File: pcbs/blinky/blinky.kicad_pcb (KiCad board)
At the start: 4 copper layers, 91 x 93 mm, 182 parts, among them J1 JACK IN, J3 CA1-9, J4 CB1-9, Q1 PMBT2222A,215, SW1 TACTILE, SW2 JS202011JCQN, U1 ATSAMD21E17, U2 MIC5225-3.3YM5, U3 TSOP36438TT, U4 IS31FL3731-SALS2

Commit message: lovely logo
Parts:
- added LOGO1: Future, Joels KiCad Footprint Library:logo-future, F.Cu at (71.8, 94.8)
- added LOGO2: Future, Joels KiCad Footprint Library:logo-turtles, F.Cu at (93.0, 94.8)
- C1: value 100uF 6.3V -> 100u
- C10, C11: value 10uF -> 10u
- C2, C7: value 1uF -> 1u
- C3, C4, C8, C9: value 0.1uF -> 0.1u
- C5: value 1.0uF -> 1.0u
- C6: value 2.2uF -> 2.2u
- R1: value 10kΩ -> 10K
- R2: value 330Ω -> 330
- R3: value 47Ω -> 47
- R4: value 470Ω -> 470

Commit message: more details
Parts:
- added FID1: Fiducial, Fiducial:Fiducial_1mm_Mask3mm, F.Cu at (131.2, 109.3)
- added FID2: Fiducial, Fiducial:Fiducial_1mm_Mask3mm, F.Cu at (44.2, 92.3)
- added FID3: Fiducial, Fiducial:Fiducial_1mm_Mask3mm, F.Cu at (44.2, 145.3)
- added H5: MountingHole, Joels KiCad Footprint Library:JCLPCB_Tooling_Hole, F.Cu at (131.2, 74.3)
- added H6: MountingHole, Joels KiCad Footprint Library:JCLPCB_Tooling_Hole, F.Cu at (131.2, 157.3)
- added H7: MountingHole, Joels KiCad Footprint Library:JCLPCB_Tooling_Hole, F.Cu at (44.2, 74.3)
- added H8: MountingHole, Joels KiCad Footprint Library:JCLPCB_Tooling_Hole, F.Cu at (44.2, 157.3)
- added H9: Lanyard Hole, MountingHole:MountingHole_2.5mm_Pad_Via, F.Cu at (82.0, 73.3)
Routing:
- net /SWCLK: track 39.1 -> 61.4 mm, vias 1 -> 2
- net /SWDIO: track 41.5 -> 58.7 mm, vias 1 -> 2
- net /A7: track 46.1 -> 44.9 mm, vias 0 -> 2
- net /~RESET: track 15.2 -> 15.0 mm, vias 1 -> 2
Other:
- board text added: "JLCJLCJLCJLC"
- board text added: "WAKING DREAMS"

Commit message: ok, well that has been sent to china
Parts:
- H9: value Lanyard Hole -> Lanyard
- moved H9 1.47 mm to (81.8, 74.8)
- moved LOGO2 0.30 mm to (92.7, 94.8)
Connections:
- H9 pad 1: (no net) -> GND
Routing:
- net GND: track 111.7 -> 420.8 mm, vias 13 -> 14
- net (no net): track 270.2 -> 0.00 mm
- net +3V3: track 107.5 -> 50.3 mm
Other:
- board text added: "SECOND PROTOTYPE 12/31/21"

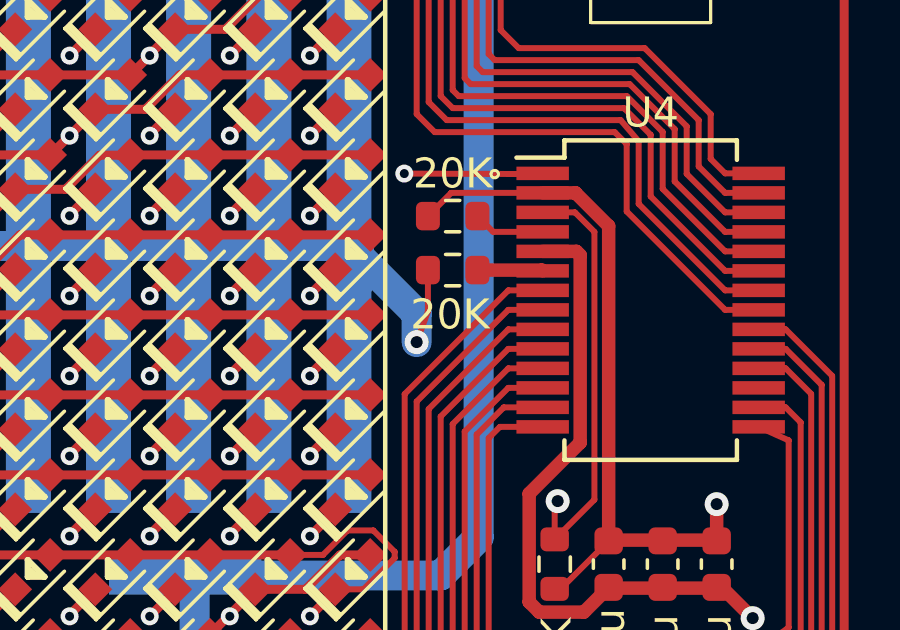
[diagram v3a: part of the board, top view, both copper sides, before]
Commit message: Use 100K resistor for Rext to save power
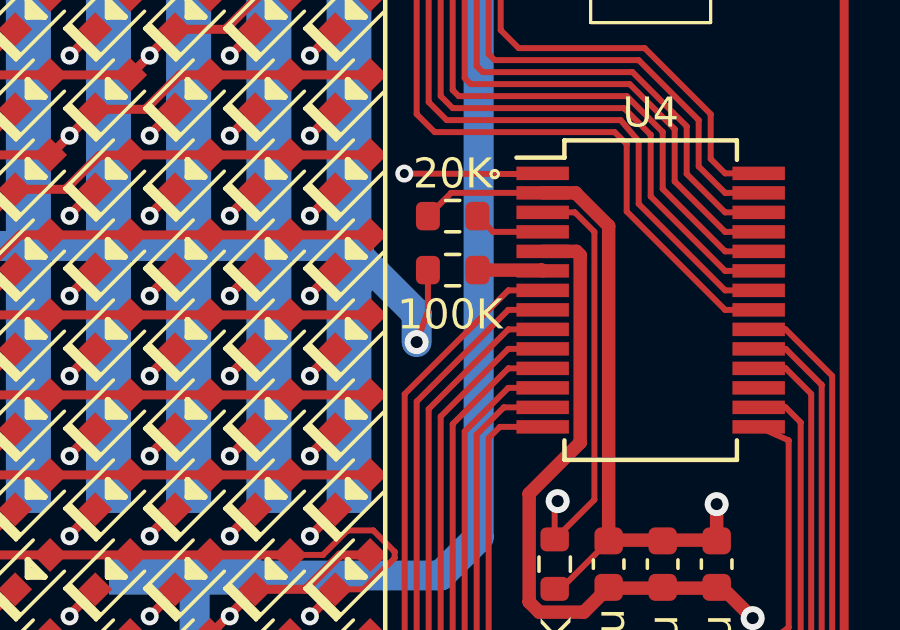
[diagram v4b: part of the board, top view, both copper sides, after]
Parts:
- R5: value 20K -> 100K

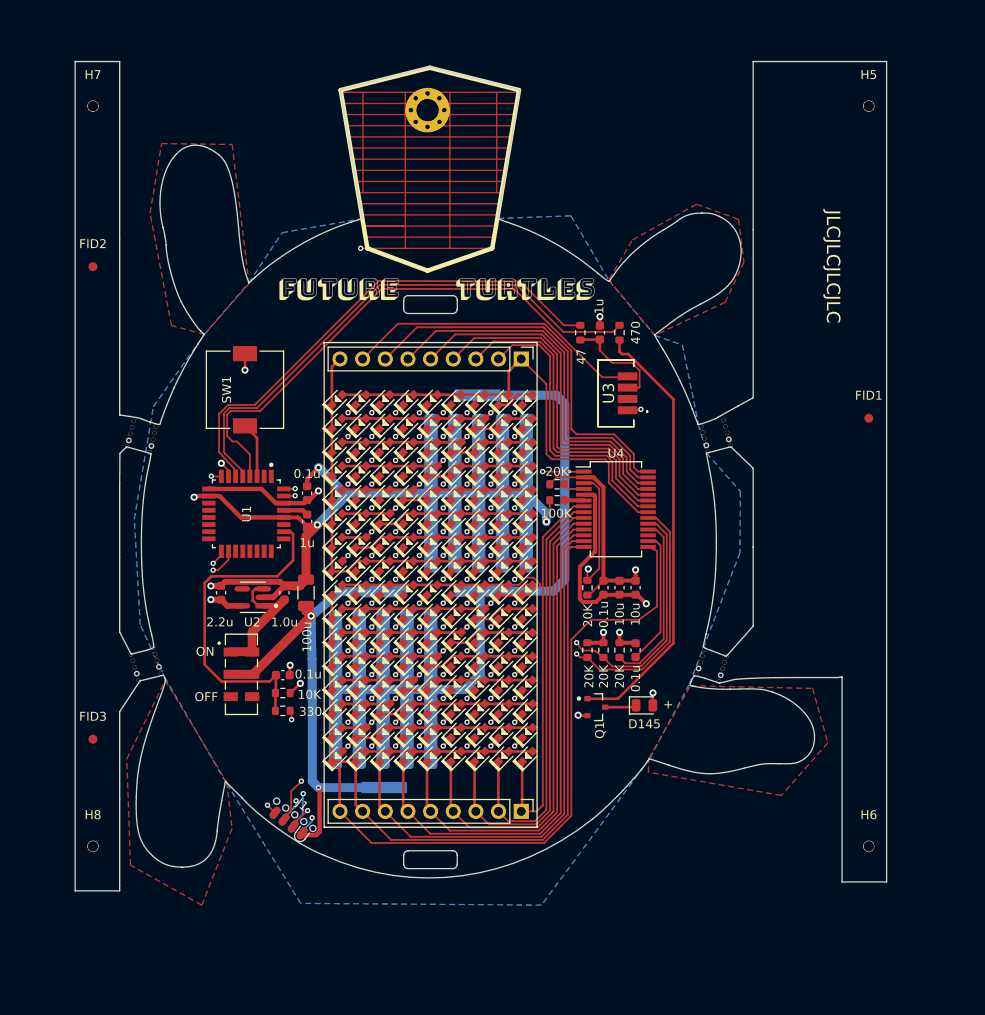
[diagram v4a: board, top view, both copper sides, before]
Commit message: Updated schematics and PCB to fix all known bugs
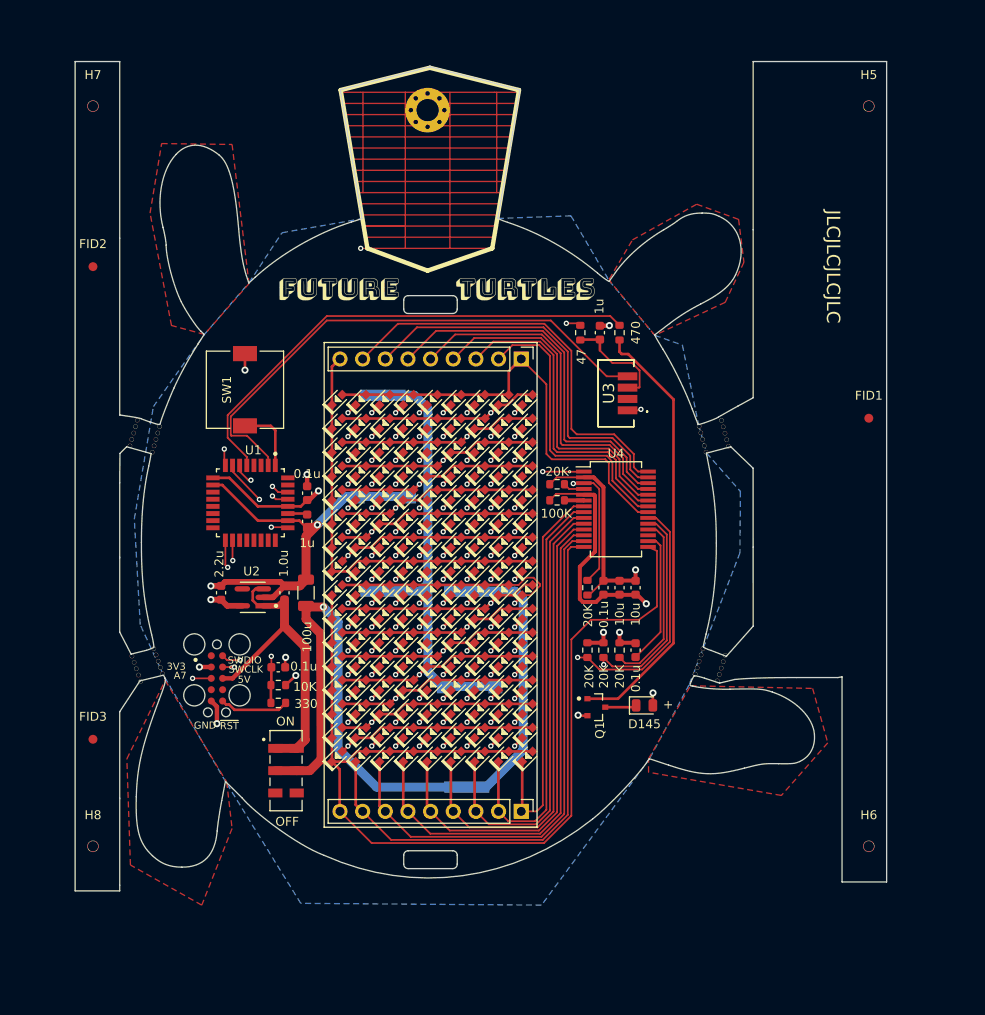
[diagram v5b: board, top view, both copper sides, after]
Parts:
- removed J1: JACK IN, Joels KiCad Footprint Library:SOIC_clipProgSmall
- added BT3: CR2032 (+) CLIP, Joels KiCad Footprint Library:BatteryHolder_Keystone_3034_Pos_Clip, B.Cu at (76.7, 117.7)
- added BT4: CR2032 (-) PAD, Joels KiCad Footprint Library:Keystone_2992_Negative_Contact_Pad, B.Cu at (80.8, 117.1)
- added J2: TC2050-IDC, Joels KiCad Footprint Library:TAG-CONNECT_TC2050-IDC, F.Cu at (58.1, 138.5)
- BT1: value CR2032 -> CR2032 (+) CLIP; footprint Joels KiCad Footprint Library:BatteryHolder_Keystone_3034_Minimum_Pad -> Joels KiCad Footprint Library:BatteryHolder_Keystone_3034_Pos_Clip
- BT2: value CR2032 -> CR2032 (-) PAD; footprint Joels KiCad Footprint Library:BatteryHolder_Keystone_3034_Minimum_Pad -> Joels KiCad Footprint Library:Keystone_2992_Negative_Contact_Pad
- U1: value ATSAMD21E17 -> ATSAMD21E17L-AF
- moved BT2 23.2 mm to (82.4, 140.4), turned to 0 degrees
- moved SW2 11.9 mm to (65.9, 148.8)
- moved BT1 9.25 mm to (86.1, 139.7), turned to 270 degrees
- moved U1 1.32 mm to (61.9, 118.8)
- moved C4 1.02 mm to (65.0, 137.2)
- moved R1 1.02 mm to (65.0, 139.2)
- moved R2 1.02 mm to (65.0, 141.2)
- moved H1 0.41 mm to (51.9, 109.5), turned to 74 degrees
- moved H3 0.24 mm to (114.5, 108.8)
- moved H4 0.18 mm to (115.3, 135.2)
- moved H2 0.12 mm to (50.8, 134.4), turned to 109 degrees
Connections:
- BT2 pad 1: Net-(BT1-Pad2) -> Net-(BT2-Pad1)
- U1 pad 1: Net-(U1-Pad1) -> /A0
- U1 pad 2: Net-(U1-Pad2) -> /A1
- U1 pad 25: Net-(U1-Pad25) -> /2RST
- U1 pad 26: /2RST -> GND
- U1 pad 27: Net-(U1-Pad27) -> /VDDCORE
- U1 pad 28: GND -> +3V3
- U1 pad 29: /VDDCORE -> /SWCLK
- U1 pad 3: /A0 -> Net-(U1-Pad3)
- U1 pad 30: +3V3 -> /SWDIO
- U1 pad 31: /SWCLK -> Net-(U1-Pad31)
- U1 pad 32: /SWDIO -> Net-(U1-Pad32)
- U1 pad 4: /A1 -> Net-(U1-Pad4)
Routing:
- net Net-(BT1-Pad2): track 65.9 -> 0.00 mm
- net Net-(BT2-Pad1): track 0.00 -> 48.8 mm
- net VBUS: track 56.3 -> 90.0 mm, vias 2 -> 1
- net /SWDIO: track 58.7 -> 28.3 mm
- net /SWCLK: track 61.4 -> 31.6 mm
- net GND: track 420.8 -> 396.8 mm, vias 14 -> 12
- net +5V: track 16.2 -> 36.2 mm
- net /A7: track 44.9 -> 32.2 mm
- net /2RST: track 37.3 -> 27.0 mm, vias 0 -> 2
- net /~RESET: track 15.0 -> 7.80 mm, vias 2 -> 0
- net /A3: track 56.4 -> 49.9 mm, vias 0 -> 2
- net /A2: track 60.8 -> 55.5 mm
- net /CA9: track 93.9 -> 90.5 mm
- net /A6: track 68.1 -> 65.7 mm
- net /A1: track 62.1 -> 59.8 mm
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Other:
- board text added: "3V3"
- board text added: "5V"
- board text added: "A7"
- board text added: "CR2032 BATTERIES FLAT (+) SIDE UP"
- board text added: "GND"
- board text added: "SWCLK"
- board text added: "SWDIO"
- board text added: "THIRD PROTOTYPE 2/20/22"
- board text added: "~RST"
- board text removed: "CR2032 BATTERY FLAT SIDE UP"
- board text removed: "SECOND PROTOTYPE 12/31/21"
